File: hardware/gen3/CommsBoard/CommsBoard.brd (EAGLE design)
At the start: 140 x 107 mm, 41 parts, among them U1 ATMEGA165PV-8AU

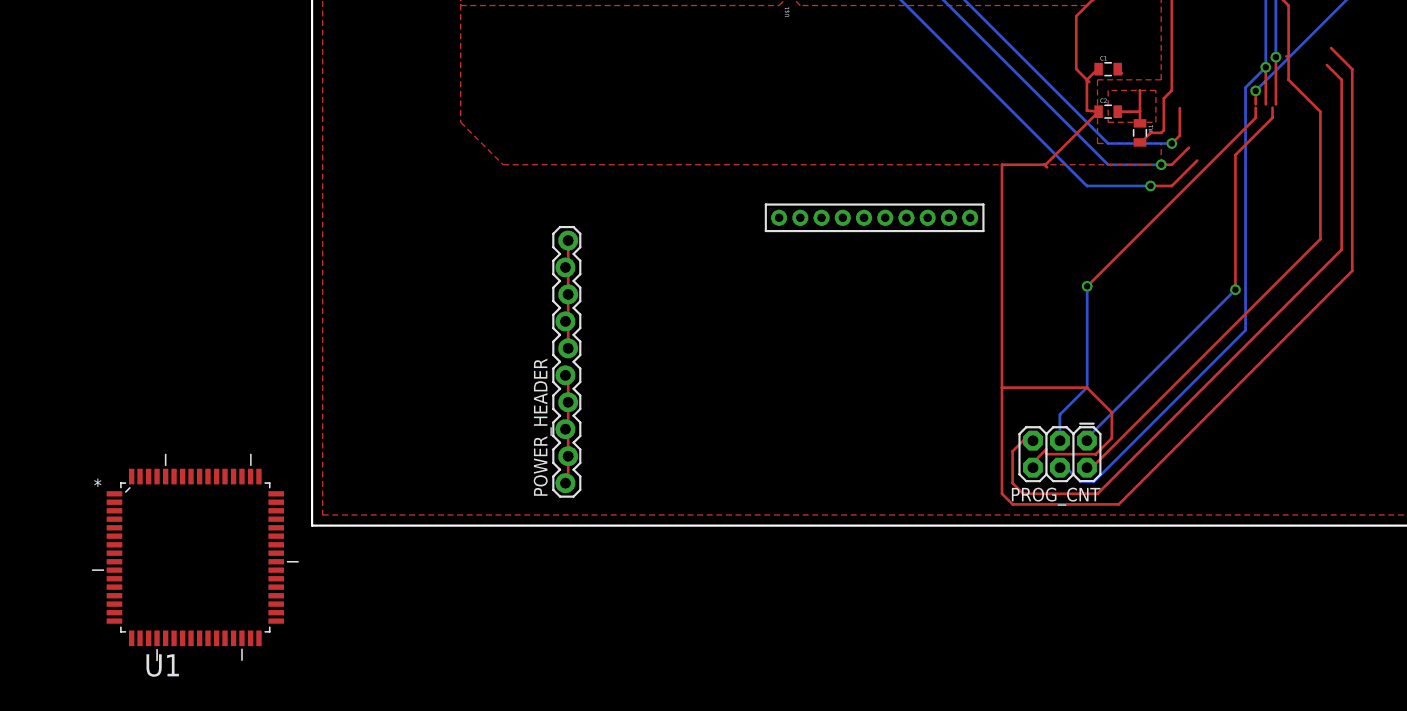
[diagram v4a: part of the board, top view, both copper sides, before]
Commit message: Added programmer port to boards
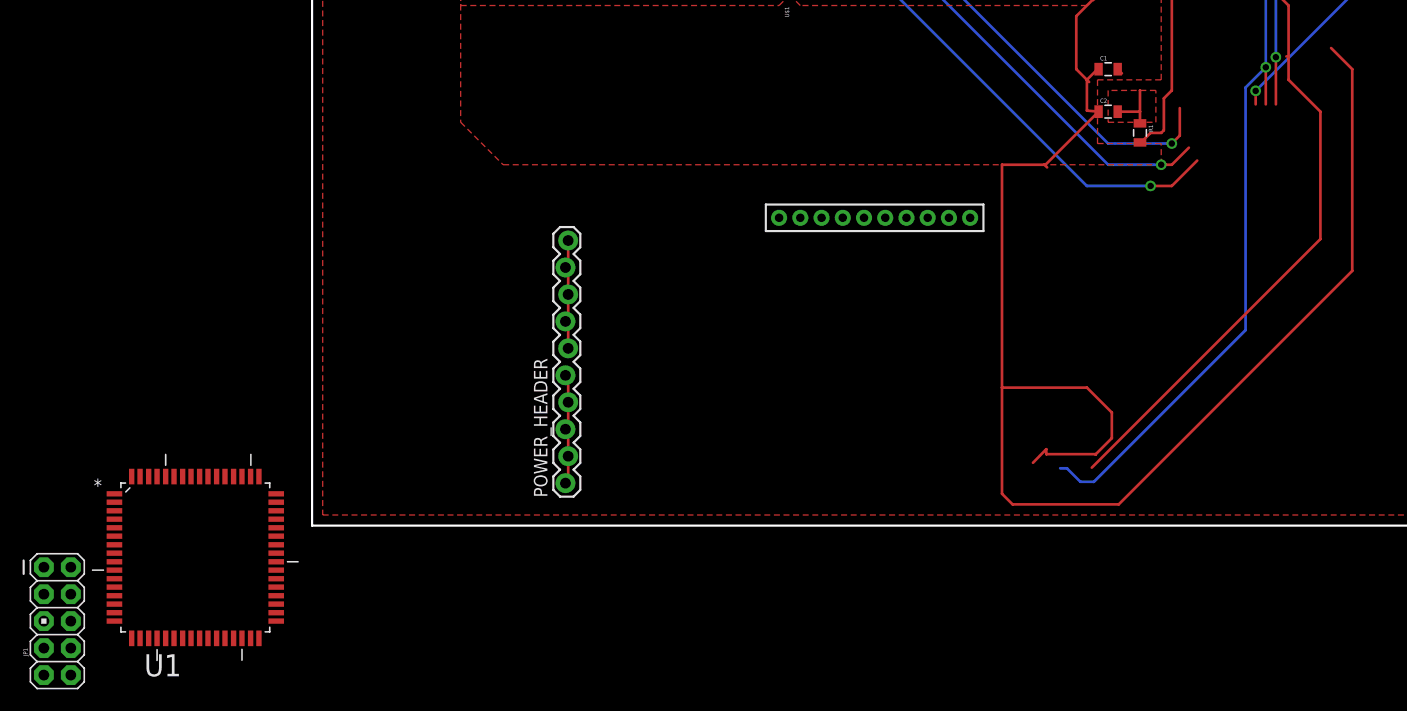
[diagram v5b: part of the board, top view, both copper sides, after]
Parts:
- removed PROG_CNT: (no value), SparkFun-Connectors:2X3
- added JP1: M05X2PTH, SparkFun-Connectors:AVR_ICSP
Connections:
- net 3.3V: now also JP1.2; no longer PROG_CNT.2
- net GND: now also JP1.10, JP1.4, JP1.6, JP1.8; no longer PROG_CNT.6
- net MISO: now also JP1.9; no longer PROG_CNT.1
- net MOSI: now also JP1.1; no longer PROG_CNT.4
- net RESET: now also JP1.5; no longer PROG_CNT.5
- net SCK: now also JP1.7; no longer PROG_CNT.3
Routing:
- net RESET: track 64.2 -> 0.00 mm
- net SCK: track 77.7 -> 38.7 mm, vias 2 -> 1
- net MISO: track 81.6 -> 42.9 mm, vias 2 -> 1
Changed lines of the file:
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@@
 <element name="R3" library="SparkFun-Passives" package="0805" value="10k" x="110" y="75" rot="MR180"/>
 <element name="R4" library="SparkFun-Passives" package="0805" value="10k" x="110" y="70" rot="MR180"/>
-<element name="PROG_CNT" library="SparkFun-Connectors" package="2X3" value="" x="73" y="8" rot="R180">
-<attribute name="PROD_ID" value="CONN-09701" x="73" y="8" size="1.778" layer="27" rot="R180" display="off"/>
-</element>
 <element name="FRAME2" library="SparkFun-Aesthetics" package="CREATIVE_COMMONS" value="FRAME-LETTER" x="88.95" y="-14.47"/>
 <element name="ROBID" library="SparkFun-Electromechanical" package="4-POS-DIP-SMD" value="4-POS-DIP" x="61" y="87" rot="R180">
@@
 <attribute name="OC_FARNELL" value="1455104" x="-11" y="-3" size="1.778" layer="27" display="off"/>
 </element>
+<element name="JP1" library="SparkFun-Connectors" package="AVR_ICSP" value="M05X2PTH" x="-24" y="-9"/>
 </elements>
 <signals>
@@
 <contactref element="C1" pad="1"/>
 <contactref element="C2" pad="1"/>
-<contactref element="PROG_CNT" pad="6"/>
 <contactref element="LOGIC_HEADER" pad="2"/>
 <contactref element="R5" pad="1"/>
@@
 <vertex x="45" y="50"/>
 </polygon>
-<wire x1="67.92" y1="5.46" x2="67.92" y2="5.92" width="0.254" layer="1"/>
 <wire x1="67.92" y1="5.92" x2="69.17" y2="7.2" width="0.254" layer="1"/>
 <wire x1="69.25" y1="33.75" x2="69" y2="34" width="0.254" layer="1"/>
@@
 <contactref element="U1" pad="22"/>
 <contactref element="U1" pad="63"/>
+<contactref element="JP1" pad="10"/>
+<contactref element="JP1" pad="8"/>
+<contactref element="JP1" pad="6"/>
+<contactref element="JP1" pad="4"/>
 <wire x1="101" y1="101.5" x2="106" y2="101.5" width="0" layer="19" extent="1-1"/>
 <wire x1="96" y1="101.5" x2="101" y2="101.5" width="0" layer="19" extent="1-1"/>
@@
 <wire x1="73" y1="75.1" x2="78" y2="75.1" width="0" layer="19" extent="1-1"/>
 <wire x1="67" y1="75.1" x2="73" y2="75.1" width="0" layer="19" extent="1-1"/>
+<wire x1="62" y1="75.1" x2="67" y2="75.1" width="0" layer="19" extent="1-1"/>
 <wire x1="68" y1="70" x2="67" y2="75.1" width="0" layer="19" extent="1-1"/>
 <wire x1="65" y1="70" x2="68" y2="70" width="0" layer="19" extent="1-1"/>
-<wire x1="61.9" y1="69" x2="65" y2="70" width="0" layer="19" extent="1-1"/>
 <wire x1="68" y1="67" x2="68" y2="70" width="0" layer="19" extent="1-1"/>
 <wire x1="65" y1="67" x2="65" y2="70" width="0" layer="19" extent="1-1"/>
+<wire x1="61.9" y1="69" x2="65" y2="70" width="0" layer="19" extent="1-1"/>
 <wire x1="61.9" y1="64" x2="65" y2="67" width="0" layer="19" extent="1-1"/>
-<wire x1="62" y1="75.1" x2="67" y2="75.1" width="0" layer="19" extent="1-1"/>
 <wire x1="73.794" y1="49.794" x2="68" y2="67" width="0" layer="19" extent="1-1"/>
 <wire x1="44" y1="51" x2="61.9" y2="64" width="0" layer="19" extent="1-1"/>
@@
 <wire x1="-8.206" y1="4.62" x2="24" y2="55" width="0" layer="19" extent="1-1"/>
 <wire x1="-16.207" y1="4.62" x2="-8.206" y2="4.62" width="0" layer="19" extent="1-1"/>
-<wire x1="-13.0066" y1="-10.62" x2="-16.207" y2="4.62" width="0" layer="19" extent="1-1"/>
+<wire x1="-22.73" y1="-6.46" x2="-16.207" y2="4.62" width="0" layer="19" extent="1-1"/>
+<wire x1="-22.73" y1="-9" x2="-22.73" y2="-6.46" width="0" layer="19" extent="1-1"/>
+<wire x1="-22.73" y1="-11.54" x2="-22.73" y2="-9" width="0" layer="19" extent="1-1"/>
+<wire x1="-22.73" y1="-14.08" x2="-22.73" y2="-11.54" width="0" layer="19" extent="1-1"/>
+<wire x1="-13.0066" y1="-10.62" x2="-22.73" y2="-11.54" width="0" layer="19" extent="1-1"/>
 </signal>
 <signal name="3.3V">
 <contactref element="R1" pad="2"/>
-<contactref element="PROG_CNT" pad="2"/>
 <contactref element="LOGIC_HEADER" pad="3"/>
 <contactref element="LOGIC_HEADER" pad="4"/>
@@
 </polygon>
 <wire x1="92" y1="44.206" x2="91.794" y2="44.206" width="0.254" layer="1"/>
-<wire x1="73" y1="5.46" x2="73.46" y2="5.46" width="0.254" layer="1"/>
 <wire x1="73.46" y1="5.46" x2="95" y2="27" width="0.254" layer="1"/>
 <wire x1="95" y1="27" x2="95" y2="39" width="0.254" layer="1"/>
@@
 <contactref element="U1" pad="21"/>
 <contactref element="U1" pad="52"/>
+<contactref element="JP1" pad="2"/>
 <wire x1="80.27" y1="91.445" x2="82.81" y2="91.445" width="0" layer="19" extent="1-1"/>
 <wire x1="77.73" y1="91.445" x2="80.27" y2="91.445" width="0" layer="19" extent="1-1"/>
@@
 <wire x1="-7.3932" y1="4.62" x2="23.873" y2="62.08" width="0" layer="19" extent="1-1"/>
 <wire x1="-13.794" y1="-10.62" x2="-7.3932" y2="4.62" width="0" layer="19" extent="1-1"/>
+<wire x1="-22.73" y1="-3.92" x2="-13.794" y2="-10.62" width="0" layer="19" extent="1-1"/>
 </signal>
 <signal name="FILT">
@@
 <signal name="MISO">
 <contactref element="R3" pad="1"/>
-<contactref element="PROG_CNT" pad="1"/>
 <wire x1="108.9025" y1="71.4375" x2="108.9025" y2="74.93" width="0.254" layer="16"/>
 <wire x1="90.805" y1="53.34" x2="108.9025" y2="71.4375" width="0.254" layer="16"/>
@@
 <wire x1="90.805" y1="39.6875" x2="90.805" y2="44.1325" width="0.254" layer="1"/>
 <wire x1="108.9025" y1="74.93" x2="109.1" y2="75" width="0.254" layer="16"/>
-<wire x1="86.995" y1="22.225" x2="73.025" y2="8.255" width="0.254" layer="16"/>
-<wire x1="86.995" y1="34.925" x2="86.995" y2="22.225" width="0.254" layer="1"/>
-<wire x1="90.4875" y1="38.4175" x2="86.995" y2="34.925" width="0.254" layer="1"/>
-<wire x1="90.4875" y1="39.37" x2="90.4875" y2="38.4175" width="0.254" layer="1"/>
-<wire x1="73.025" y1="8.255" x2="73" y2="8" width="0.254" layer="16"/>
 <via x="90.805" y="44.1325" extent="1-16" drill="0.6096"/>
-<via x="86.995" y="22.225" extent="1-16" drill="0.6096"/>
 <contactref element="U1" pad="13"/>
-<wire x1="90.4875" y1="39.37" x2="90.805" y2="39.6875" width="0" layer="19" extent="1-1"/>
-<wire x1="-18.62" y1="-6.6068" x2="73" y2="8" width="0" layer="19" extent="1-1"/>
+<contactref element="JP1" pad="9"/>
+<wire x1="-18.62" y1="-6.6068" x2="90.805" y2="39.6875" width="0" layer="19" extent="1-1"/>
+<wire x1="-25.27" y1="-14.08" x2="-18.62" y2="-6.6068" width="0" layer="19" extent="1-1"/>
 </signal>
 <signal name="SCK">
 <contactref element="R4" pad="1"/>
-<contactref element="PROG_CNT" pad="3"/>
-<wire x1="70.46" y1="8" x2="70.46" y2="10.46" width="0.254" layer="16"/>
-<wire x1="70.46" y1="10.46" x2="73" y2="13" width="0.254" layer="16"/>
 <wire x1="108.9025" y1="60.96" x2="108.9025" y2="69.85" width="0.254" layer="16"/>
 <wire x1="88.9" y1="40.9575" x2="108.9025" y2="60.96" width="0.254" layer="16"/>
 <wire x1="88.9" y1="39.6875" x2="88.9" y2="40.9575" width="0.254" layer="1"/>
 <wire x1="108.9025" y1="69.85" x2="109.1" y2="70" width="0.254" layer="16"/>
-<wire x1="73.025" y1="22.5425" x2="73.025" y2="13.0175" width="0.254" layer="16"/>
-<wire x1="88.9" y1="38.4175" x2="73.025" y2="22.5425" width="0.254" layer="1"/>
-<wire x1="88.9" y1="39.37" x2="88.9" y2="38.4175" width="0.254" layer="1"/>
-<wire x1="73.025" y1="13.0175" x2="73" y2="13" width="0.254" layer="16"/>
 <via x="88.9" y="40.9575" extent="1-16" drill="0.6096"/>
-<via x="73.025" y="22.5425" extent="1-16" drill="0.6096"/>
 <contactref element="U1" pad="11"/>
-<wire x1="88.9" y1="39.37" x2="88.9" y2="39.6875" width="0" layer="19" extent="1-1"/>
-<wire x1="-18.62" y1="-5.0066" x2="70.46" y2="8" width="0" layer="19" extent="1-1"/>
+<contactref element="JP1" pad="7"/>
+<wire x1="-18.62" y1="-5.0066" x2="88.9" y2="39.6875" width="0" layer="19" extent="1-1"/>
+<wire x1="-25.27" y1="-11.54" x2="-18.62" y2="-5.0066" width="0" layer="19" extent="1-1"/>
 </signal>
 <signal name="SS_M">
@@
 <signal name="MOSI">
 <contactref element="R2" pad="1"/>
-<contactref element="PROG_CNT" pad="4"/>
 <wire x1="108.9025" y1="76.5175" x2="108.9025" y2="79.6925" width="0.254" layer="16"/>
 <wire x1="89.8525" y1="57.4675" x2="108.9025" y2="76.5175" width="0.254" layer="16"/>
@@
 <wire x1="87.9475" y1="41.275" x2="87.9475" y2="18.415" width="0.254" layer="16"/>
 <wire x1="89.8525" y1="43.18" x2="87.9475" y2="41.275" width="0.254" layer="16"/>
-<wire x1="70.485" y1="5.3975" x2="70.46" y2="5.46" width="0.254" layer="16"/>
 <via x="89.8525" y="43.18" extent="1-16" drill="0.6096"/>
 <contactref element="U1" pad="12"/>
-<wire x1="-18.62" y1="-5.794" x2="70.46" y2="5.46" width="0" layer="19" extent="1-1"/>
+<contactref element="JP1" pad="1"/>
+<wire x1="-18.62" y1="-5.794" x2="70.485" y2="5.3975" width="0" layer="19" extent="1-16"/>
+<wire x1="-25.27" y1="-3.92" x2="-18.62" y2="-5.794" width="0" layer="19" extent="1-1"/>
 </signal>
 <signal name="N$3">
@@
 </signal>
 <signal name="RESET">
-<contactref element="PROG_CNT" pad="5"/>
-<wire x1="95.6068" y1="43.3932" x2="97" y2="42" width="0.254" layer="1"/>
-<wire x1="97" y1="42" x2="97" y2="26" width="0.254" layer="1"/>
-<wire x1="97" y1="26" x2="74" y2="3" width="0.254" layer="1"/>
-<wire x1="74" y1="3" x2="67" y2="3" width="0.254" layer="1"/>
-<wire x1="67" y1="3" x2="66" y2="4" width="0.254" layer="1"/>
-<wire x1="66" y1="4" x2="66" y2="7" width="0.254" layer="1"/>
-<wire x1="66" y1="7" x2="67" y2="8" width="0.254" layer="1"/>
-<wire x1="67" y1="8" x2="67.92" y2="8" width="0.254" layer="1"/>
 <contactref element="U1" pad="20"/>
-<wire x1="-14.6068" y1="-10.62" x2="66" y2="4" width="0" layer="19" extent="1-1"/>
+<contactref element="JP1" pad="5"/>
+<wire x1="-14.6068" y1="-10.62" x2="-25.27" y2="-9" width="0" layer="19" extent="1-1"/>
 </signal>
 <signal name="12V">

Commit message: connected RTS and CTS on xbee
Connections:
- new net CTS: U$1.12, U1.6
- new net RTS: U$1.16, U1.5
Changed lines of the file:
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@@
 <setting verticaltext="up"/>
 </settings>
-<grid distance="1" unitdist="mm" unit="mm" style="lines" multiple="1" display="yes" altdistance="0.01" altunitdist="mm" altunit="mm"/>
+<grid distance="0.05" unitdist="inch" unit="inch" style="lines" multiple="1" display="yes" altdistance="0.01" altunitdist="mm" altunit="mm"/>
 <layers>
 <layer number="1" name="Top" color="4" fill="1" visible="yes" active="yes"/>
@@
 <wire x1="34" y1="98.5" x2="34" y2="81.28" width="0.254" layer="1"/>
 </signal>
+<signal name="RTS">
+<contactref element="U$1" pad="16"/>
+<contactref element="U1" pad="5"/>
+<wire x1="-18.62" y1="-0.206" x2="54" y2="29" width="0" layer="19" extent="1-1"/>
+</signal>
+<signal name="CTS">
+<contactref element="U$1" pad="12"/>
+<contactref element="U1" pad="6"/>
+<wire x1="-18.62" y1="-0.9934" x2="46" y2="29" width="0" layer="19" extent="1-1"/>
+</signal>
 </signals>
